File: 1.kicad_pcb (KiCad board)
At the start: 2 copper layers, 7 parts, among them Q1 BC107, Q2 BC107, Q3 BC107, Q4 BC107

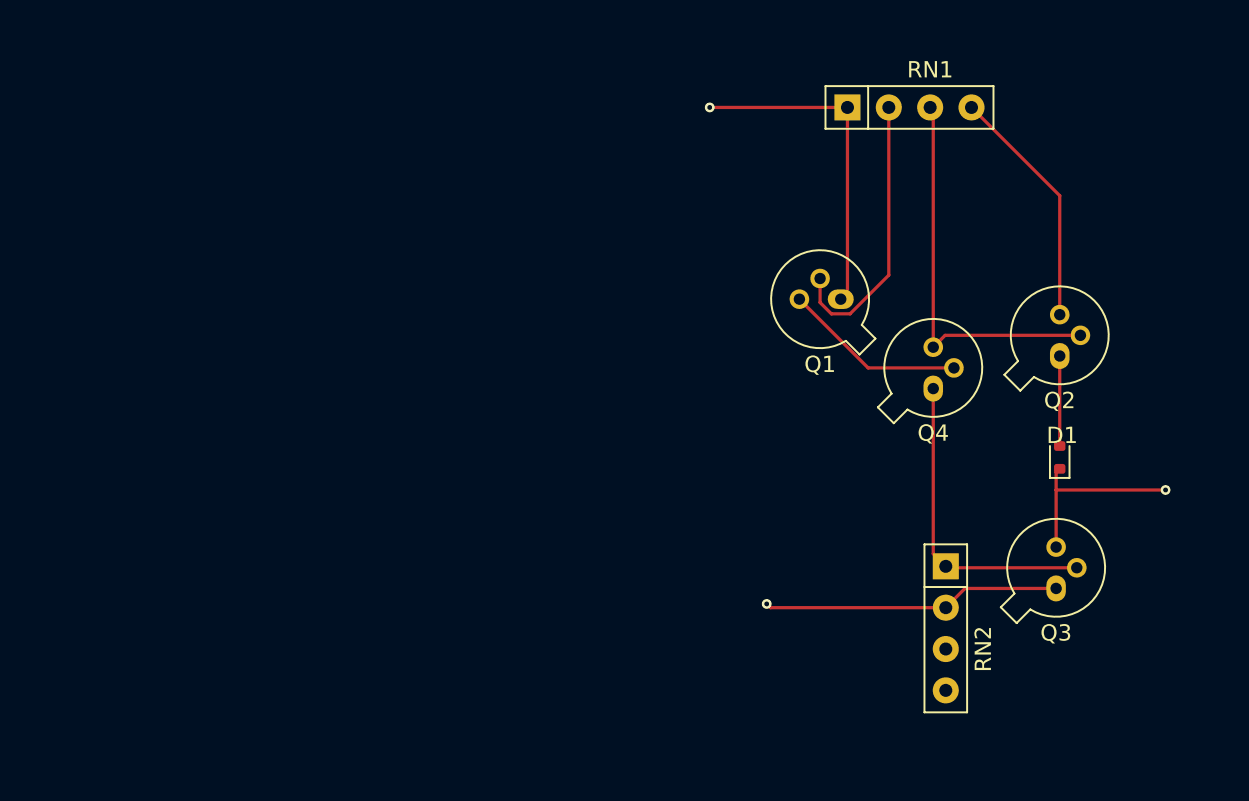
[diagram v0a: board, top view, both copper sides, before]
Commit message: 1-create_basic_NAND_logic_discrete_gate: Create correct basic NAND gate schematic.
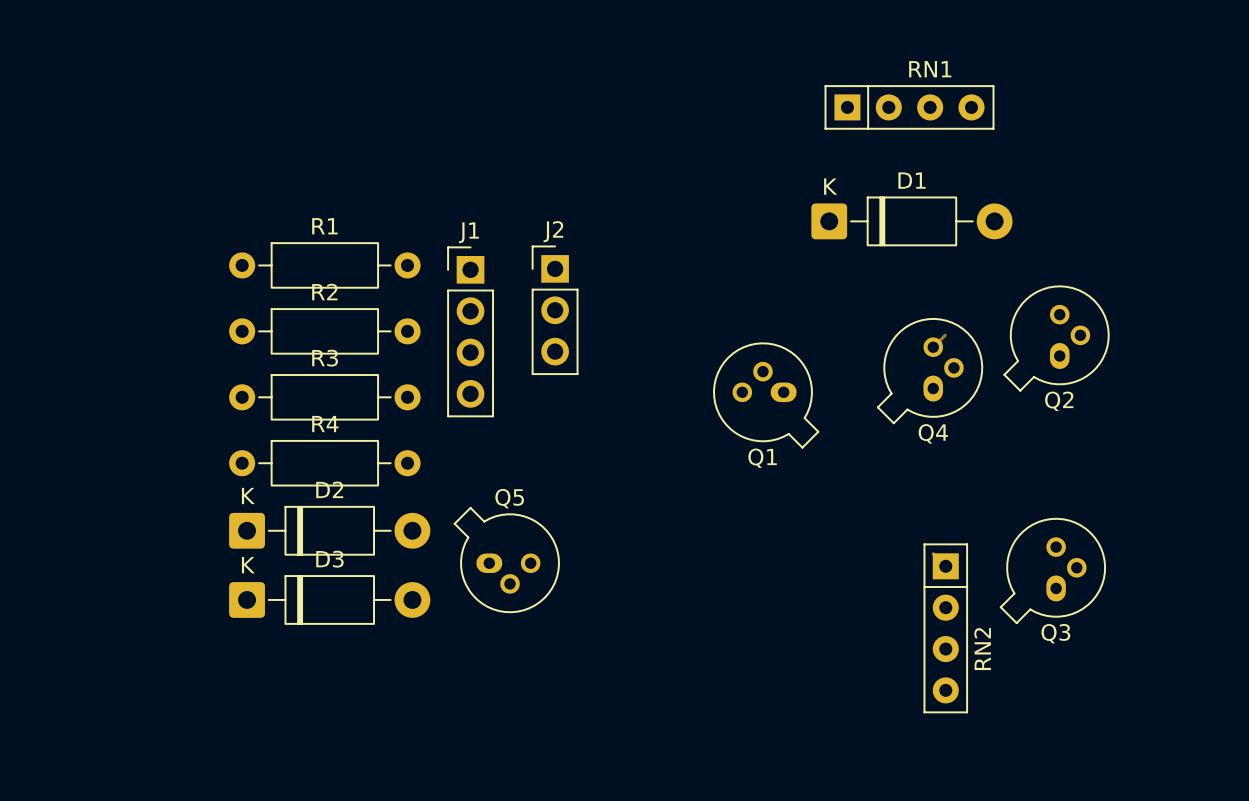
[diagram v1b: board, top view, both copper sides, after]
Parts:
- added D2: 1N4007, Diode_THT:D_DO-41_SOD81_P10.16mm_Horizontal, F.Cu at (68.1, 60.5)
- added D3: 1N4007, Diode_THT:D_DO-41_SOD81_P10.16mm_Horizontal, F.Cu at (68.1, 64.8)
- added J1: Conn_01x04_Pin, Connector_PinHeader_2.54mm:PinHeader_1x04_P2.54mm_Vertical, F.Cu at (81.8, 44.5)
- added J2: Conn_01x03_Pin, Connector_PinHeader_2.54mm:PinHeader_1x03_P2.54mm_Vertical, F.Cu at (87.0, 44.4)
- added Q5: BC107, Package_TO_SOT_THT:TO-18-3, F.Cu at (83.0, 62.5)
- added R1: 1K, Resistor_THT:R_Axial_DIN0207_L6.3mm_D2.5mm_P10.16mm_Horizontal, F.Cu at (67.8, 44.2)
- added R2: 130R, Resistor_THT:R_Axial_DIN0207_L6.3mm_D2.5mm_P10.16mm_Horizontal, F.Cu at (67.8, 48.3)
- added R3: 1K6, Resistor_THT:R_Axial_DIN0207_L6.3mm_D2.5mm_P10.16mm_Horizontal, F.Cu at (67.8, 52.3)
- added R4: 4 K, Resistor_THT:R_Axial_DIN0207_L6.3mm_D2.5mm_P10.16mm_Horizontal, F.Cu at (67.8, 56.4)
- D1: value 1N4148WT -> 1N4007; footprint Diode_SMD:D_SOD-523 -> Diode_THT:D_DO-41_SOD81_P10.16mm_Horizontal
- moved D1 20.3 mm to (103.8, 41.5), turned to 0 degrees
- moved Q1 6.71 mm to (101.0, 52.0)
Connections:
- net +3.3V renamed Net-(D1-K)
- Q1 pad 1: +5V -> Net-(D3-K)
- Q3 pad 1: GNDREF -> GND
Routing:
- net Net-(Q2-B): track 24.2 -> 1.30 mm
- net +5V: track 20.4 -> 0.00 mm, vias 1 -> 0
- net GNDREF: track 18.4 -> 0.00 mm, vias 1 -> 0
- net Net-(Q3-B): track 19.3 -> 1.21 mm
- net Net-(Q1-B): track 17.3 -> 0.00 mm
- net Net-(Q2-C): track 15.0 -> 0.00 mm
- net Net-(D1-K): track 11.9 -> 0.31 mm, vias 1 -> 0
- net Net-(Q1-C): track 11.2 -> 0.00 mm
- net Net-(D1-A): track 5.53 -> 0.00 mm

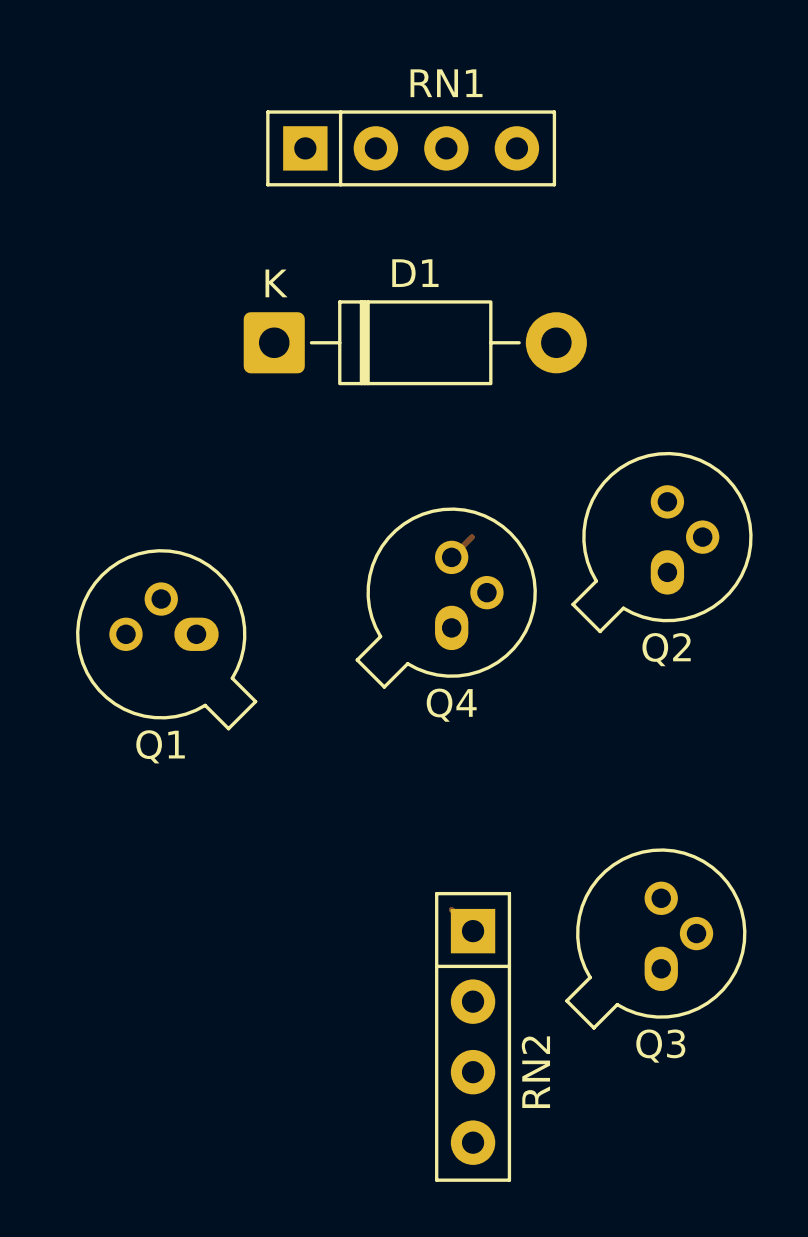
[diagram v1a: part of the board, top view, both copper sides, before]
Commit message: 1-create_basic_NAND_logic_discrete_gate: Delete trash resistors in 3d model.
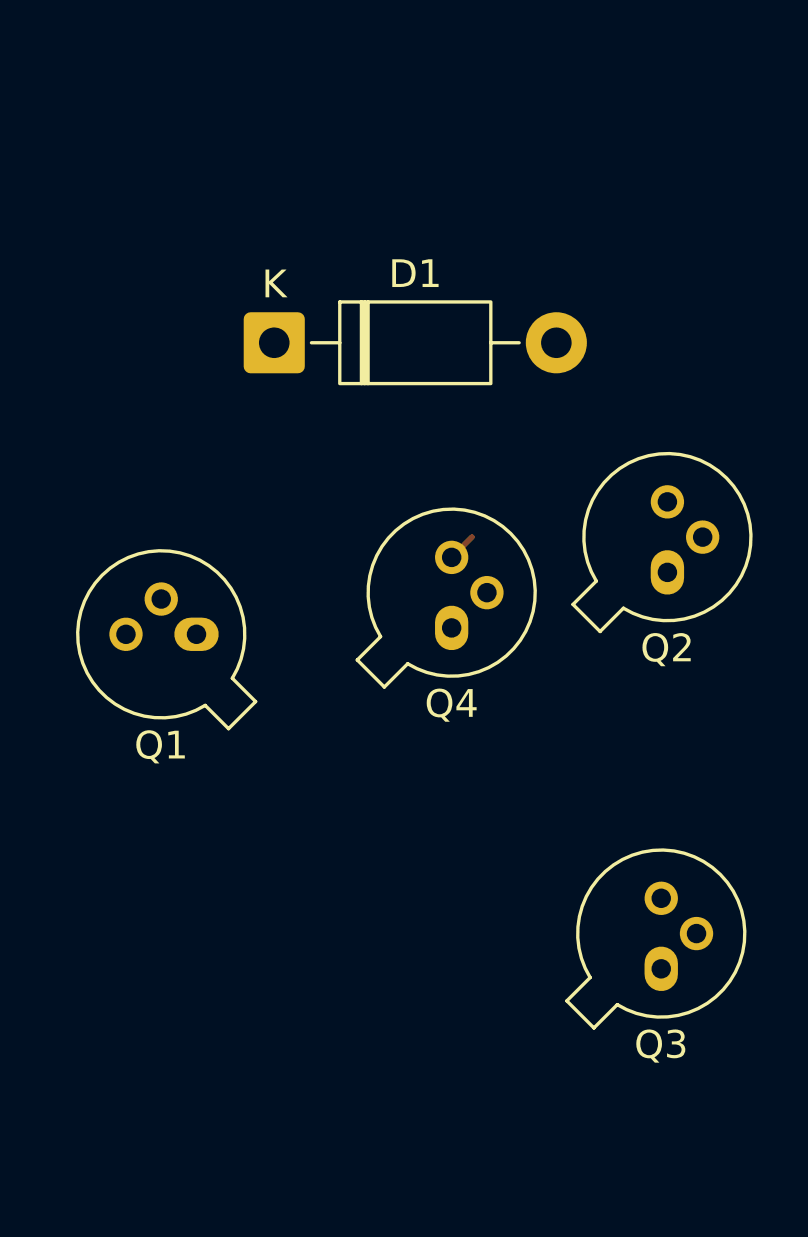
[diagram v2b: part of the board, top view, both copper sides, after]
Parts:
- removed RN1, RN2: R_Network03_Split, Resistor_THT:R_Array_SIP4
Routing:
- net Net-(Q3-B): track 1.21 -> 0.00 mm

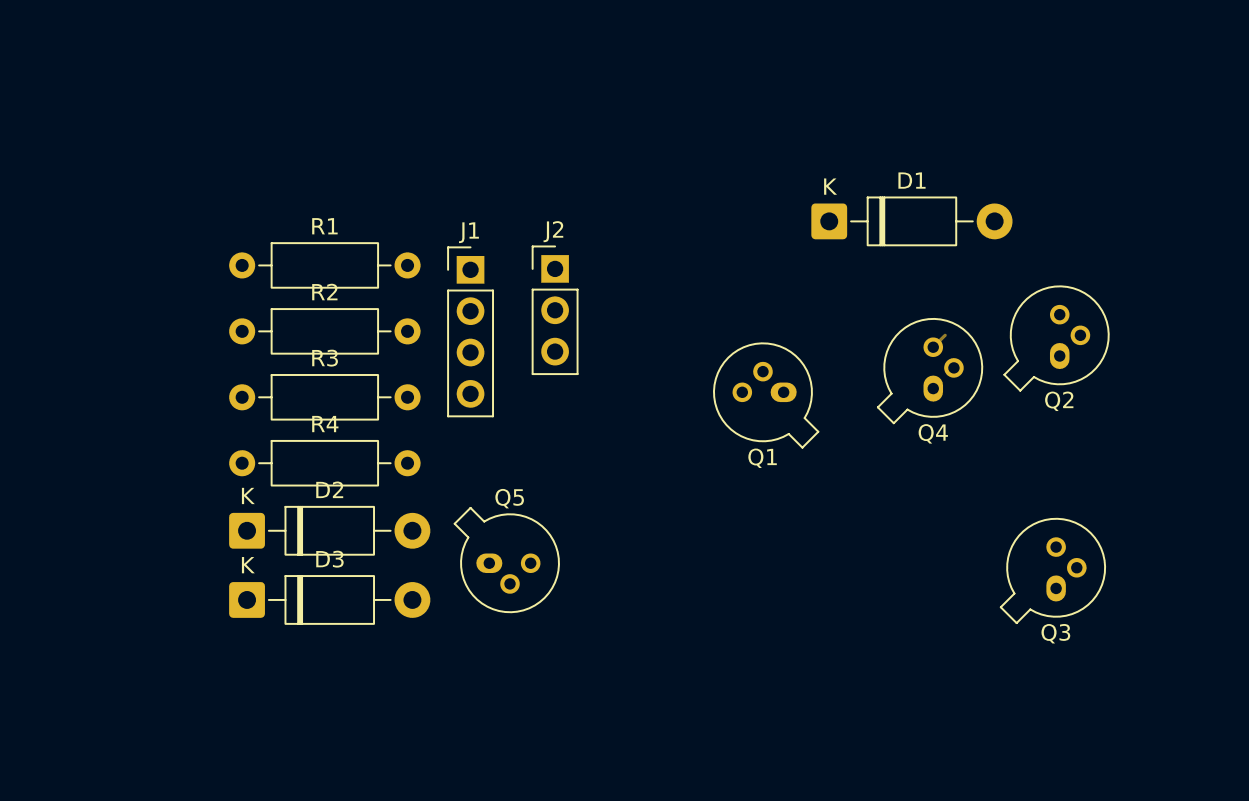
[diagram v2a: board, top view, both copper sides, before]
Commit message: 1-create_basic_NAND_logic_discrete_gate: Added board border.
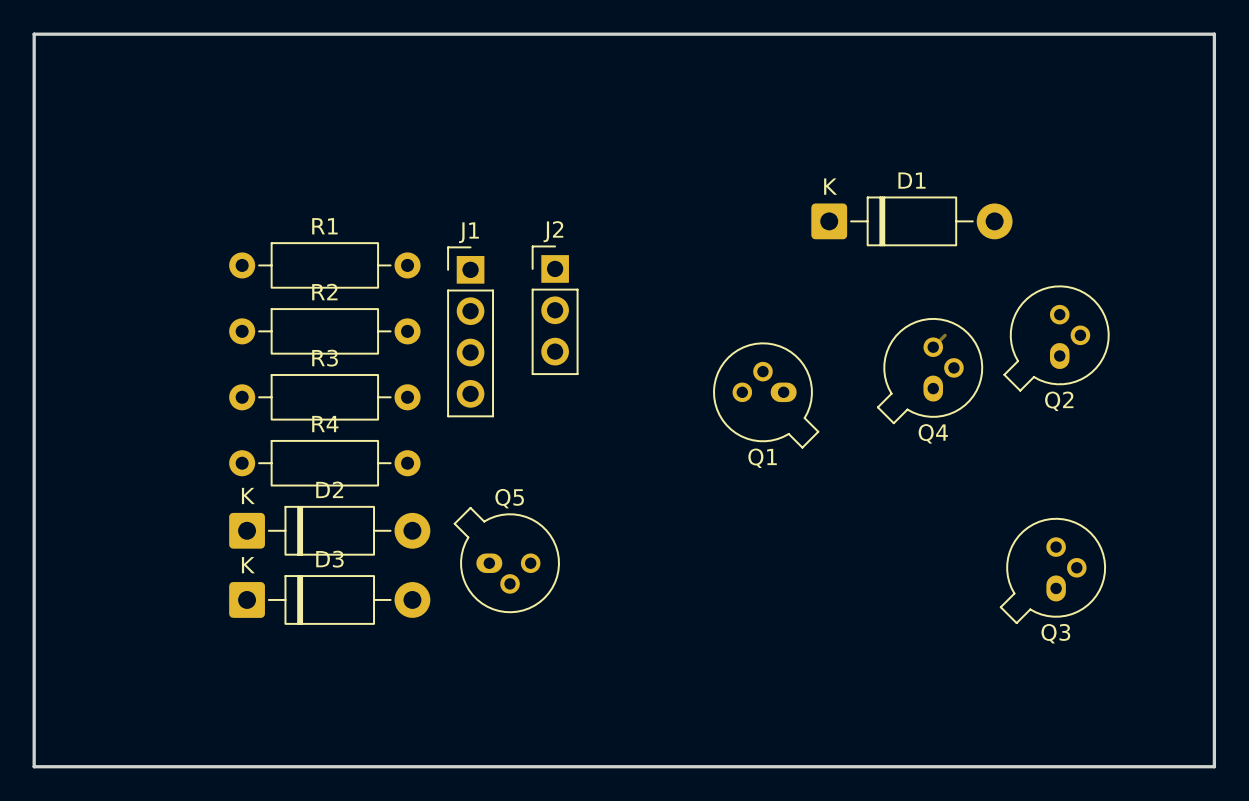
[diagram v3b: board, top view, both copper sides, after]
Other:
- board outline added: 72.5 x 45 mm
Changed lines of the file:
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@@
 		)
+	)
+	(gr_line
+		(start 127.5 75)
+		(end 55 75)
+		(stroke
+			(width 0.2)
+			(type solid)
+		)
+		(layer "Edge.Cuts")
+	)
+	(gr_line
+		(start 55 30)
+		(end 55 75)
+		(stroke
+			(width 0.2)
+			(type solid)
+		)
+		(layer "Edge.Cuts")
+	)
+	(gr_line
+		(start 127.5 30)
+		(end 127.5 75)
+		(stroke
+			(width 0.2)
+			(type solid)
+		)
+		(layer "Edge.Cuts")
+	)
+	(gr_line
+		(start 55 30)
+		(end 127.5 30)
+		(stroke
+			(width 0.2)
+			(type solid)
+		)
+		(layer "Edge.Cuts")
 	)
 	(segment
